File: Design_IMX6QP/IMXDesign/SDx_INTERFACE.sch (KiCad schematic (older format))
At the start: 0 parts

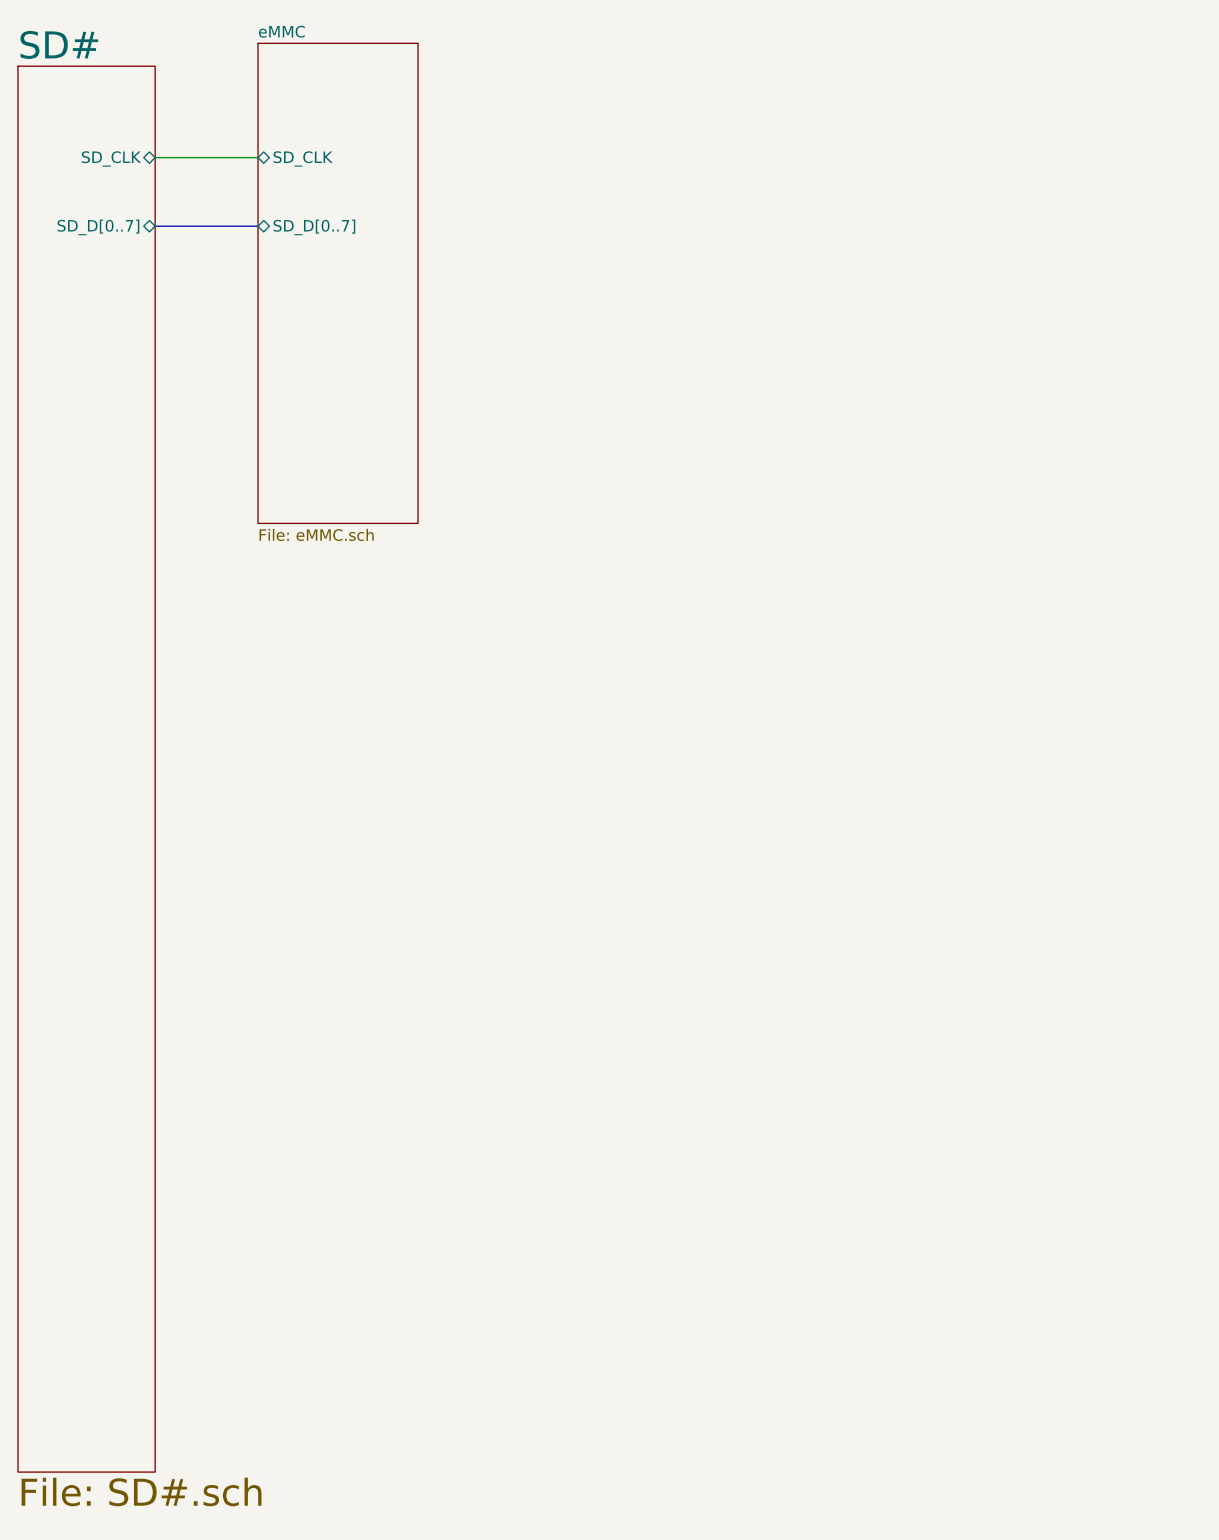
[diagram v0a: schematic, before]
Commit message: Update IMX6QP and IMX8MQ
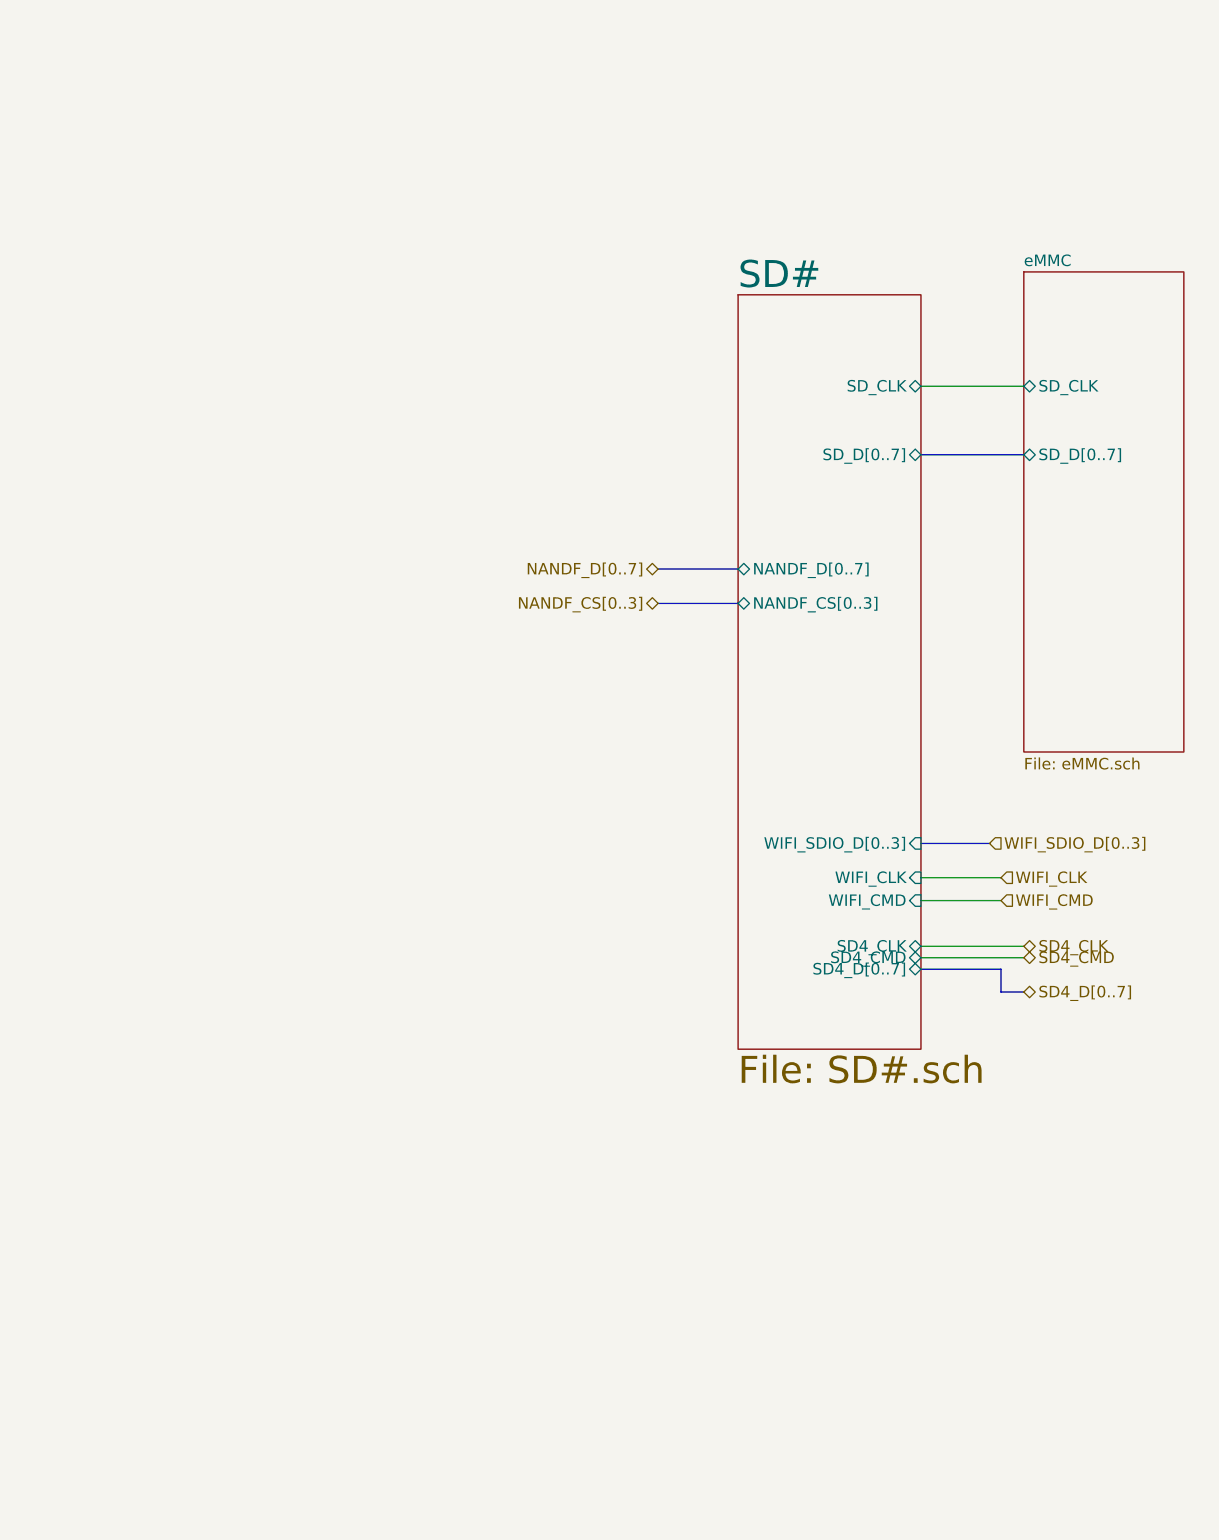
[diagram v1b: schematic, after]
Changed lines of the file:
@@
 $Descr A4 11693 8268
 encoding utf-8
-Sheet 6 12
+Sheet 11 17
 Title ""
 Date ""
@@
 $EndDescr
 Wire Bus Line
-	1500 1900 1950 1900
+	4850 2900 5300 2900
 Wire Wire Line
-	1500 1600 1950 1600
+	4850 2600 5300 2600
 $Sheet
-S 900  1200 600  6150
+S 5300 2100 700  2100
+U 60E57310
+F0 "eMMC" 50
+F1 "eMMC.sch" 50
+F2 "SD_CLK" B L 5300 2600 50
+F3 "SD_D[0..7]" B L 5300 2900 50
+$EndSheet
+Wire Wire Line
+	5200 4850 4850 4850
+Wire Wire Line
+	4850 4750 5200 4750
+Text HLabel 5200 4750 2    50   Input ~ 0
+WIFI_CLK
+Text HLabel 5200 4850 2    50   Input ~ 0
+WIFI_CMD
+Text HLabel 5150 4600 2    50   Input ~ 0
+WIFI_SDIO_D[0..3]
+Wire Bus Line
+	4850 4600 5150 4600
+Wire Wire Line
+	4850 5050 5300 5050
+Text HLabel 5300 5050 2    50   BiDi ~ 0
+SD4_CLK
+Text HLabel 5300 5250 2    50   BiDi ~ 0
+SD4_D[0..7]
+Wire Wire Line
+	4850 5100 5300 5100
+Text HLabel 5300 5100 2    50   BiDi ~ 0
+SD4_CMD
+$Sheet
+S 4050 2200 800  3300
 U 60D2D67D
 F0 "SD#" 118
 F1 "SD#.sch" 118
-F2 "SD_CLK" B R 1500 1600 50
-F3 "SD_D[0..7]" B R 1500 1900 50
+F2 "SD_CLK" B R 4850 2600 50
+F3 "SD_D[0..7]" B R 4850 2900 50
+F4 "WIFI_SDIO_D[0..3]" I R 4850 4600 50
+F5 "WIFI_CLK" I R 4850 4750 50
+F6 "WIFI_CMD" I R 4850 4850 50
+F7 "SD4_CLK" B R 4850 5050 50
+F8 "SD4_D[0..7]" B R 4850 5150 50
+F9 "SD4_CMD" B R 4850 5100 50
+F10 "NANDF_D[0..7]" B L 4050 3400 50
+F11 "NANDF_CS[0..3]" B L 4050 3550 50
 $EndSheet
-$Sheet
-S 1950 1100 700  2100
-U 60E57310
-F0 "eMMC" 50
-F1 "eMMC.sch" 50
-F2 "SD_CLK" B L 1950 1600 50
-F3 "SD_D[0..7]" B L 1950 1900 50
-$EndSheet
+Wire Bus Line
+	4850 5150 5200 5150
+Wire Bus Line
+	5200 5150 5200 5250
+Wire Bus Line
+	5200 5250 5300 5250
+Text HLabel 3700 3400 0    50   BiDi ~ 0
+NANDF_D[0..7]
+Wire Bus Line
+	4050 3400 3700 3400
+Text HLabel 3700 3550 0    50   BiDi ~ 0
+NANDF_CS[0..3]
+Wire Bus Line
+	4050 3550 3700 3550
 $EndSCHEMATC
